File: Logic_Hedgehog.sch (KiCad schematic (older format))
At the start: 11 parts

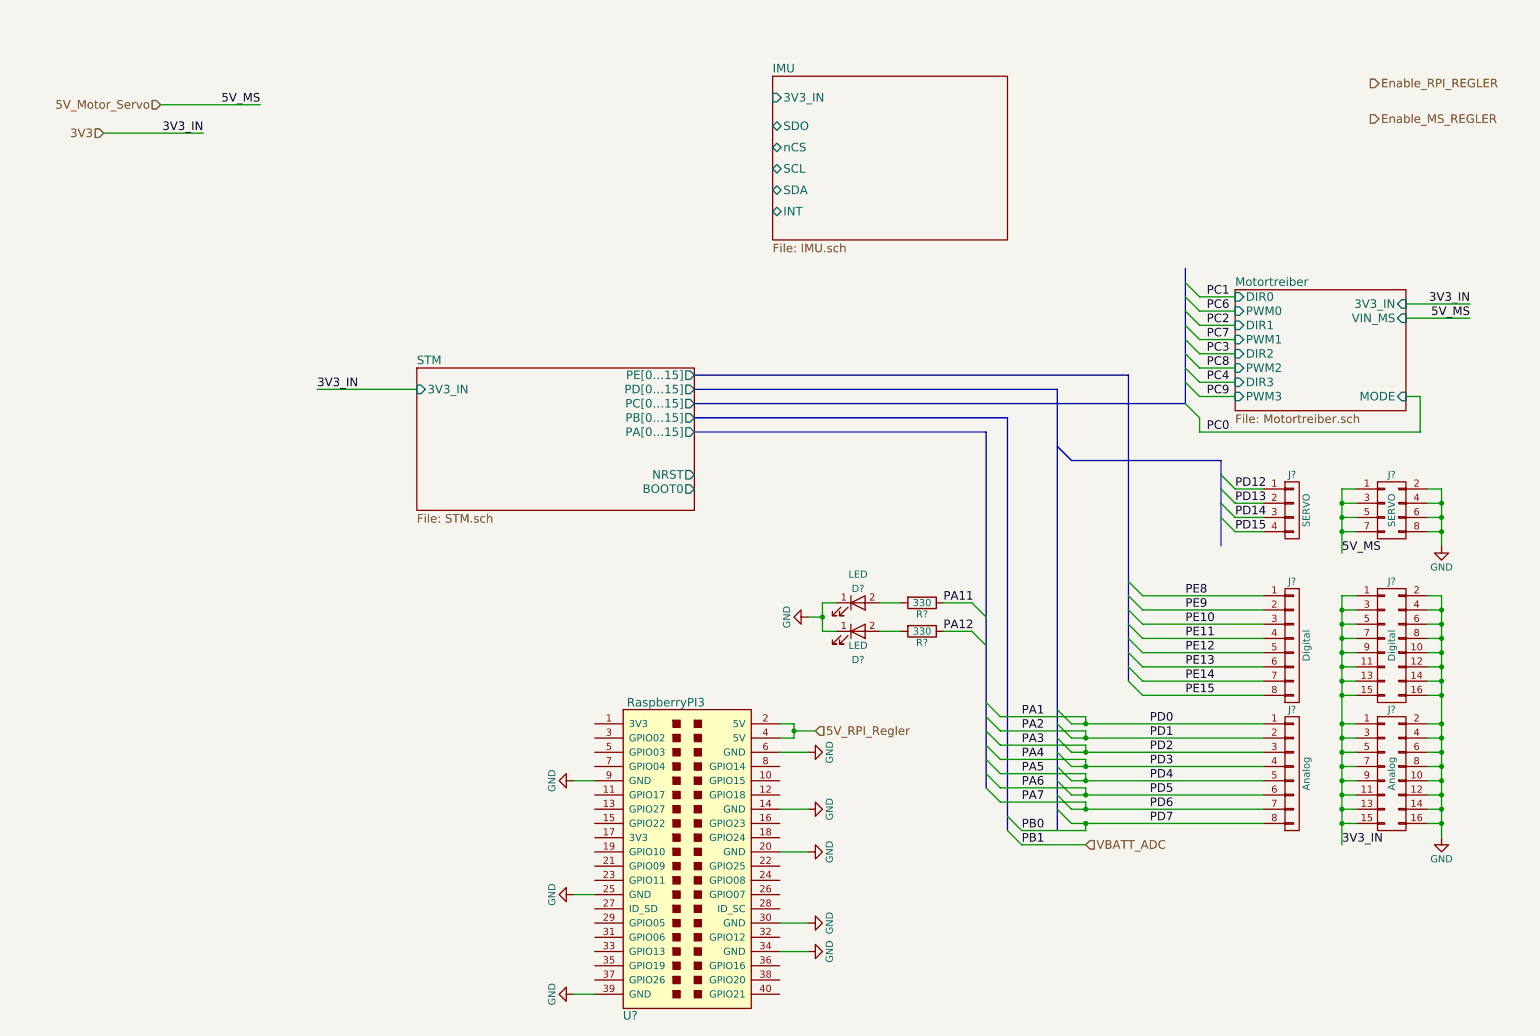
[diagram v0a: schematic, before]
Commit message: Added Piezo Buzzer in Libray Added Piezo Buzzer schematic Added Pinout for STM32 SWDIO / JTAG is missing
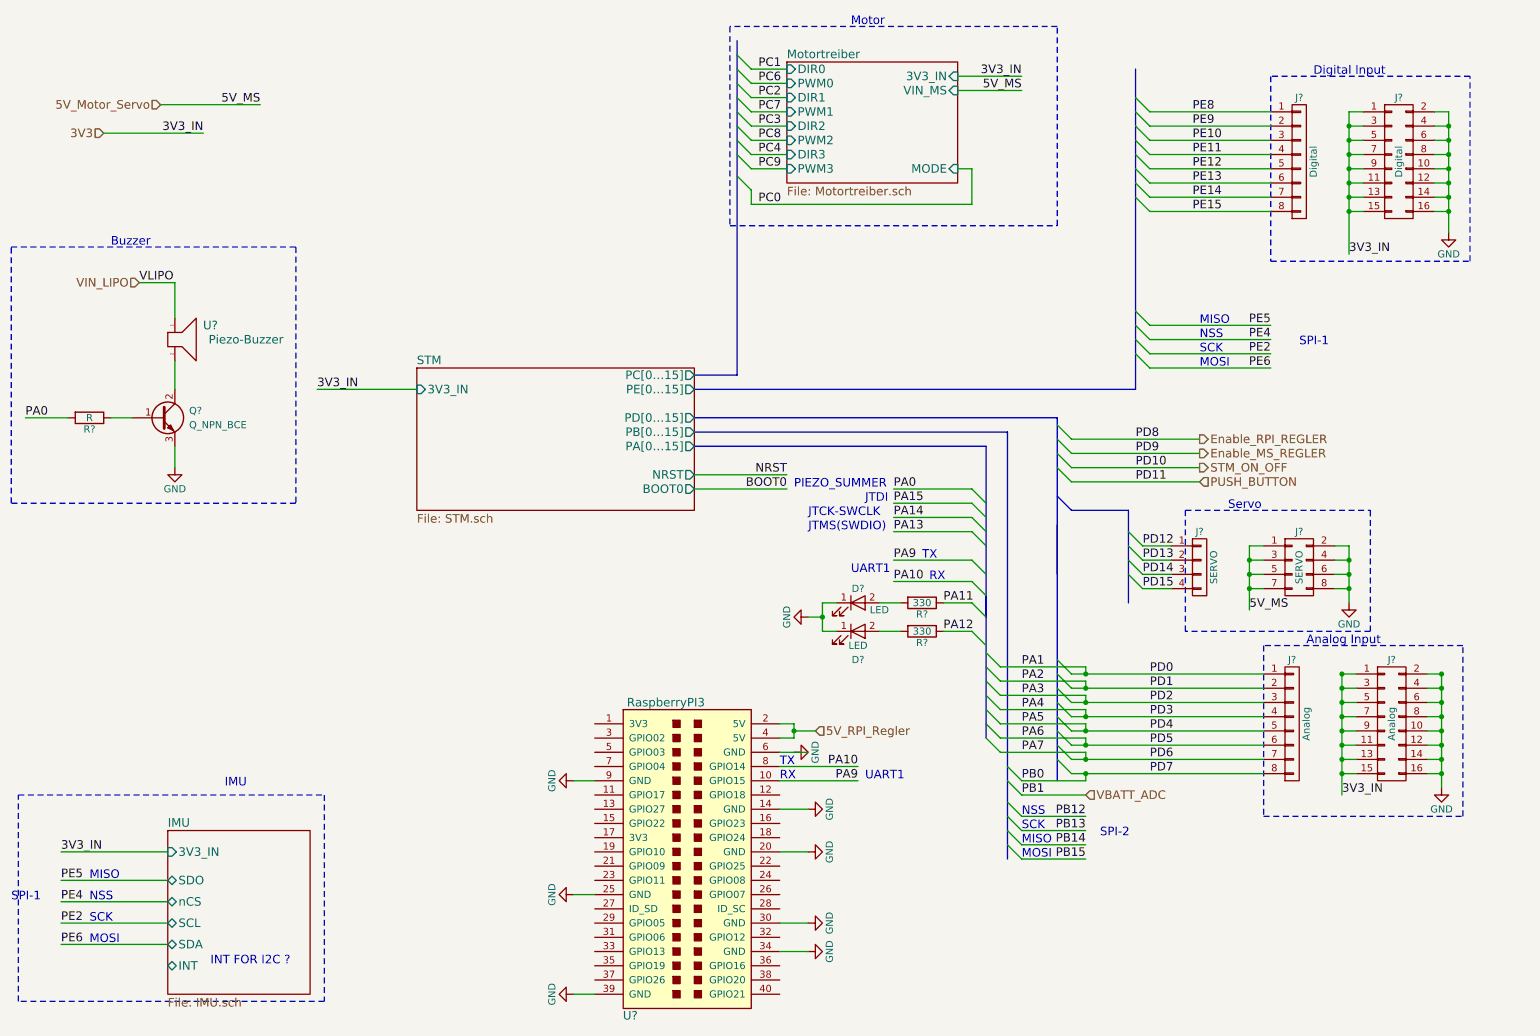
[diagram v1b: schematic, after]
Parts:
- added Q?: Q_NPN_BCE, symbol Q_NPN_BCE
- added R?: R, symbol R
- added U?: Piezo-Buzzer, symbol Piezo-Buzzer
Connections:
- net GND: now also Q?.3 (E); no longer U?.6 (GND)
- net PA9: now reaches U?.10 (GPIO15)
- net PA10: now reaches U?.8 (GPIO14)
- new net: Q?.2 (C), U?.2
- new net: Q?.1 (B), R?.1
- new net PA0: R?.2
- new net VIN_LIPO: U?.1
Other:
- note added: "Analog Input"
- note added: "Buzzer"
- note added: "Digital Input"
- note added: "IMU"
- note added: "INT FOR I2C ?"
- note added: "JTCK-SWCLK"
- note added: "JTDI"
- note added: "JTMS(SWDIO)"
- note added: "MISO"
- note added: "MOSI"
- note added: "Motor"
- note added: "NSS"
- note added: "PIEZO_SUMMER"
- note added: "RX"
- note added: "SCK"
- note added: "SPI-1"
- note added: "SPI-2"
- note added: "Servo"
- note added: "TX"
- note added: "UART1"
- moved on the sheet: J?

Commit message: cleanup
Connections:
- net VIN_LIPO is gone; now on net +3V3: U?.1
- net 3V3 renamed +3V3
- net 5V_Motor_Servo renamed +5V
- net 5V_RPI_Regler renamed 5V_RPi
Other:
- note added: "SPI1"
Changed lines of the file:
@@
 LIBS:valves
 LIBS:hedgehog_symbols
+LIBS:switches
 LIBS:Hedgehog-cache
-EELAYER 25 0
+EELAYER 26 0
 EELAYER END
 $Descr A4 11693 8268
@@
 $EndDescr
 Text HLabel 6350 5600 2    60   Input ~ 0
-5V_RPI_Regler
-Text HLabel 1750 1200 0    60   Input ~ 0
-5V_Motor_Servo
-Text HLabel 1350 1400 0    60   Input ~ 0
+5V_RPi
+Text HLabel 1700 1500 0    60   Input ~ 0
+5V_MS
+Text HLabel 1700 1775 0    60   Input ~ 0
 3V3
 Text HLabel 9050 3550 2    60   Output ~ 0
-Enable_RPI_REGLER
+EN_Reg_RPi
 Text HLabel 9050 3650 2    60   Output ~ 0
-Enable_MS_REGLER
+EN_Reg_MS
 $Sheet
 S 3550 3050 1950 1000
@@
 F12 "MODE" I R 7350 1650 60
 $EndSheet
-Text Label 2050 1400 2    60   ~ 0
-3V3_IN
-Text Label 2850 3200 0    60   ~ 0
-3V3_IN
-Text Label 7800 1000 2    60   ~ 0
-3V3_IN
-Text Label 2450 1200 2    60   ~ 0
-5V_MS
-Text Label 7800 1100 2    60   ~ 0
-5V_MS
 $Comp
 L RaspberryPI3 U?
@@
 	1    0    0    -1
 $EndComp
-Text Label 9400 4750 0    60   ~ 0
-5V_MS
 $Comp
 L GND #PWR?
@@
 	1    0    0    -1
 $EndComp
-Text Label 10050 6050 0    60   ~ 0
-3V3_IN
 Entry Wire Line
 	8600 1150 8700 1250
@@
 PB1
 Text HLabel 8250 6050 2    60   Input ~ 0
-VBATT_ADC
+POWER_IN_SENSE
 Entry Wire Line
 	5800 850  5900 950
@@
 $EndSheet
 Text HLabel 9050 3750 2    60   Output ~ 0
-STM_ON_OFF
+EN_PWR_IN
 Text HLabel 9050 3850 2    60   Input ~ 0
-PUSH_BUTTON
+PWR_BUTTON_STATE
 Text Notes 2100 7250 0    60   ~ 0
 INT FOR I2C ?
 Wire Wire Line
-	1350 1400 2050 1400
-Wire Wire Line
-	3550 3200 2850 3200
-Wire Wire Line
-	7350 1000 7800 1000
-Wire Wire Line
-	1750 1200 2450 1200
-Wire Wire Line
-	7350 1100 7800 1100
-Wire Wire Line
 	6100 5550 6200 5550
 Wire Wire Line
@@
 Wire Wire Line
 	9400 4600 9500 4600
-Wire Wire Line
-	9400 4300 9400 4750
 Wire Wire Line
 	9400 4300 9500 4300
@@
 Connection ~ 10050 5900
 Wire Wire Line
-	10100 1250 10100 2250
-Wire Wire Line
-	10050 5200 10050 6050
-Wire Wire Line
 	8700 1250 9550 1250
 Wire Wire Line
@@
 	1050 6800 1800 6800
 Wire Wire Line
-	1800 6450 1050 6450
-Wire Wire Line
 	1800 6650 1050 6650
 Wire Wire Line
@@
 Wire Wire Line
 	1800 7100 1050 7100
-Text Label 1050 6450 0    60   ~ 0
-3V3_IN
 Text Label 1050 6650 0    60   ~ 0
 PE5
@@
 	1    0    0    -1
 $EndComp
-Text Label 10100 2250 0    60   ~ 0
-3V3_IN
 Entry Wire Line
 	8050 3450 8150 3550
@@
 Text Notes 6600 4500 0    60   ~ 0
 UART1
-Text Notes 700  6800 0    60   ~ 0
-SPI-1
+Text Notes 775  6800 0    60   ~ 0
+SPI1
 Entry Wire Line
 	7700 6100 7800 6200
@@
 Wire Wire Line
 	1850 3600 1850 3750
-Wire Wire Line
-	1850 2700 1850 2450
 $Comp
 L R R?
@@
 Wire Wire Line
 	1100 3400 800  3400
-Wire Wire Line
-	1850 2450 1600 2450
-Text Label 1600 2450 0    60   ~ 0
-VLIPO
-Text HLabel 1600 2450 0    60   Input ~ 0
-VIN_LIPO
 Text Label 800  3400 0    60   ~ 0
 PA0
@@
 Wire Notes Line
 	700  2200 2700 2200
+$Comp
+L +3V3 #PWR?
+U 1 1 59094422
+P 1775 1725
+F 0 "#PWR?" H 1775 1575 50  0001 C CNN
+F 1 "+3V3" H 1775 1875 50  0000 C CNN
+F 2 "" H 1775 1725 50  0001 C CNN
+F 3 "" H 1775 1725 50  0001 C CNN
+	1    1775 1725
+	1    0    0    -1
+$EndComp
+Wire Wire Line
+	1775 1725 1775 1775
+Wire Wire Line
+	1775 1775 1700 1775
+$Comp
+L +3V3 #PWR?
+U 1 1 59094E31
+P 1850 2600
+F 0 "#PWR?" H 1850 2450 50  0001 C CNN
+F 1 "+3V3" H 1850 2750 50  0000 C CNN
+F 2 "" H 1850 2600 50  0001 C CNN
+F 3 "" H 1850 2600 50  0001 C CNN
+	1    1850 2600
+	1    0    0    -1
+$EndComp
+Wire Wire Line
+	1850 2600 1850 2700
+$Comp
+L +3V3 #PWR?
+U 1 1 590959B1
+P 3375 3125
+F 0 "#PWR?" H 3375 2975 50  0001 C CNN
+F 1 "+3V3" H 3375 3275 50  0000 C CNN
+F 2 "" H 3375 3125 50  0001 C CNN
+F 3 "" H 3375 3125 50  0001 C CNN
+	1    3375 3125
+	1    0    0    -1
+$EndComp
+Wire Wire Line
+	3375 3125 3375 3200
+Wire Wire Line
+	3375 3200 3550 3200
+$Comp
+L +3V3 #PWR?
+U 1 1 59095ED7
+P 1575 6375
+F 0 "#PWR?" H 1575 6225 50  0001 C CNN
+F 1 "+3V3" H 1575 6525 50  0000 C CNN
+F 2 "" H 1575 6375 50  0001 C CNN
+F 3 "" H 1575 6375 50  0001 C CNN
+	1    1575 6375
+	1    0    0    -1
+$EndComp
+Wire Wire Line
+	1575 6375 1575 6450
+Wire Wire Line
+	1575 6450 1800 6450
+$Comp
+L +3V3 #PWR?
+U 1 1 59096BAF
+P 10050 5150
+F 0 "#PWR?" H 10050 5000 50  0001 C CNN
+F 1 "+3V3" H 10175 5250 50  0000 C CNN
+F 2 "" H 10050 5150 50  0001 C CNN
+F 3 "" H 10050 5150 50  0001 C CNN
+	1    10050 5150
+	1    0    0    -1
+$EndComp
+Wire Wire Line
+	10050 5150 10050 5900
+$Comp
+L +3V3 #PWR?
+U 1 1 5909B6DB
+P 10100 1200
+F 0 "#PWR?" H 10100 1050 50  0001 C CNN
+F 1 "+3V3" H 10100 1350 50  0000 C CNN
+F 2 "" H 10100 1200 50  0001 C CNN
+F 3 "" H 10100 1200 50  0001 C CNN
+	1    10100 1200
+	1    0    0    -1
+$EndComp
+Connection ~ 10100 1250
+Wire Wire Line
+	10100 1200 10100 1950
+$Comp
+L +3V3 #PWR?
+U 1 1 5909E6BA
+P 7450 925
+F 0 "#PWR?" H 7450 775 50  0001 C CNN
+F 1 "+3V3" H 7450 1075 50  0000 C CNN
+F 2 "" H 7450 925 50  0001 C CNN
+F 3 "" H 7450 925 50  0001 C CNN
+	1    7450 925
+	1    0    0    -1
+$EndComp
+Wire Wire Line
+	7450 925  7450 1000
+Wire Wire Line
+	7450 1000 7350 1000
+$Comp
+L +5V #PWR?
+U 1 1 590A3BB0
+P 1775 1450
+F 0 "#PWR?" H 1775 1300 50  0001 C CNN
+F 1 "+5V" H 1775 1600 50  0000 C CNN
+F 2 "" H 1775 1450 50  0001 C CNN
+F 3 "" H 1775 1450 50  0001 C CNN
+	1    1775 1450
+	1    0    0    -1
+$EndComp
+Wire Wire Line
+	1700 1500 1775 1500
+Wire Wire Line
+	1775 1500 1775 1450
+$Comp
+L +5V #PWR?
+U 1 1 590A40B0
+P 7650 925
+F 0 "#PWR?" H 7650 775 50  0001 C CNN
+F 1 "+5V" H 7650 1075 50  0000 C CNN
+F 2 "" H 7650 925 50  0001 C CNN
+F 3 "" H 7650 925 50  0001 C CNN
+	1    7650 925
+	1    0    0    -1
+$EndComp
+Wire Wire Line
+	7650 925  7650 1100
+Wire Wire Line
+	7650 1100 7350 1100
+$Comp
+L +5V #PWR?
+U 1 1 590A66E3
+P 9400 4250
+F 0 "#PWR?" H 9400 4100 50  0001 C CNN
+F 1 "+5V" H 9400 4400 50  0000 C CNN
+F 2 "" H 9400 4250 50  0001 C CNN
+F 3 "" H 9400 4250 50  0001 C CNN
+	1    9400 4250
+	1    0    0    -1
+$EndComp
+Wire Wire Line
+	9400 4250 9400 4600
+Connection ~ 9400 4300
 $EndSCHEMATC

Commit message: more cleanup
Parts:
- removed Q?: Q_NPN_BCE, symbol Q_NPN_BCE
- removed R?: R, symbol R
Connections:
- net +3V3: no longer U?.1
- net PA0: now also U?.1
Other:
- note added: "Piezo-Buzzer"
- note added: "Problem: 2 net names"
- note added: "SPI2"
- note added: "TODO: Timer1"
- note removed: "PIEZO_SUMMER"
- note removed: "SPI-1"
- note removed: "SPI-2"
- moved on the sheet: U?
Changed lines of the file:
@@
 S 6150 900  1200 850
 U 58F5B6C4
-F0 "Motortreiber" 60
-F1 "Motortreiber.sch" 60
+F0 "Motor_Drivers" 60
+F1 "Motor_Drivers.sch" 60
 F2 "3V3_IN" I R 7350 1000 60
 F3 "VIN_MS" I R 7350 1100 60
-F4 "DIR0" I L 6150 950 60
-F5 "DIR1" I L 6150 1150 60
-F6 "DIR2" I L 6150 1350 60
-F7 "DIR3" I L 6150 1550 60
-F8 "PWM0" I L 6150 1050 60
-F9 "PWM1" I L 6150 1250 60
-F10 "PWM2" I L 6150 1450 60
-F11 "PWM3" I L 6150 1650 60
-F12 "MODE" I R 7350 1650 60
+F4 "M0_1" I L 6150 950 60
+F5 "M1_1" I L 6150 1150 60
+F6 "M2_1" I L 6150 1350 60
+F7 "M3_1" I L 6150 1550 60
+F8 "M0_2" I L 6150 1050 60
+F9 "M1_2" I L 6150 1250 60
+F10 "M2_2" I L 6150 1450 60
+F11 "M3_2" I L 6150 1650 60
+F12 "MODE01" I R 7350 1650 60
+F13 "MODE23" I R 7350 1550 60
 $EndSheet
 $Comp
@@
 Entry Wire Line
 	5800 1550 5900 1650
-Entry Wire Line
-	5800 1700 5900 1800
 Text Label 5950 1900 0    60   ~ 0
 PC0
@@
 	5900 1650 6150 1650
 Wire Wire Line
-	5900 1800 5900 1900
-Wire Wire Line
 	5900 1900 7450 1900
 Wire Wire Line
@@
 Text Label 8250 6500 2    60   ~ 0
 PB15
-Text Notes 8350 6350 0    60   ~ 0
-SPI-2
+Text Notes 8300 6350 0    60   ~ 0
+SPI2
 Text Notes 7100 4400 0    60   ~ 0
 TX
@@
 Text Notes 9050 3050 0    60   ~ 0
 MOSI
-Text Notes 9750 2900 0    60   ~ 0
-SPI-1
+Text Notes 9600 2900 0    60   ~ 0
+SPI1
 Wire Wire Line
 	5500 3900 6150 3900
@@
 Text Label 6900 3900 0    60   ~ 0
 PA0
-Text Notes 6200 3900 0    60   ~ 0
-PIEZO_SUMMER
+Text Notes 6275 3900 0    60   ~ 0
+Piezo-Buzzer
 $Comp
 L Piezo-Buzzer U?
 U 1 1 58FC2F9F
-P 1900 2850
-F 0 "U?" H 2100 2950 60  0000 C CNN
-F 1 "Piezo-Buzzer" H 2350 2850 60  0000 C CNN
-F 2 "" H 1900 2850 60  0001 C CNN
-F 3 "" H 1900 2850 60  0001 C CNN
-	1    1900 2850
-	1    0    0    -1
-$EndComp
-$Comp
-L Q_NPN_BCE Q?
-U 1 1 58FC3920
-P 1750 3400
-F 0 "Q?" H 1950 3450 50  0000 L CNN
-F 1 "Q_NPN_BCE" H 1950 3350 50  0000 L CNN
-F 2 "" H 1950 3500 50  0001 C CNN
-F 3 "" H 1750 3400 50  0001 C CNN
-	1    1750 3400
-	1    0    0    -1
-$EndComp
-Wire Wire Line
-	1850 3000 1850 3200
-Wire Wire Line
-	1550 3400 1400 3400
-$Comp
-L GND #PWR?
-U 1 1 58FC43D7
-P 1850 3750
-F 0 "#PWR?" H 1850 3500 50  0001 C CNN
-F 1 "GND" H 1850 3600 50  0000 C CNN
-F 2 "" H 1850 3750 50  0001 C CNN
-F 3 "" H 1850 3750 50  0001 C CNN
-	1    1850 3750
-	1    0    0    -1
-$EndComp
-Wire Wire Line
-	1850 3600 1850 3750
-$Comp
-L R R?
-U 1 1 58FC530A
-P 1250 3400
-F 0 "R?" V 1330 3400 50  0000 C CNN
-F 1 "R" V 1250 3400 50  0000 C CNN
-F 2 "" V 1180 3400 50  0001 C CNN
-F 3 "" H 1250 3400 50  0001 C CNN
-	1    1250 3400
-	0    1    1    0
-$EndComp
-Wire Wire Line
-	1100 3400 800  3400
-Text Label 800  3400 0    60   ~ 0
+P 1750 3075
+F 0 "U?" H 1950 3175 60  0000 C CNN
+F 1 "Piezo-Buzzer" H 2200 3075 60  0000 C CNN
+F 2 "" H 1750 3075 60  0001 C CNN
+F 3 "" H 1750 3075 60  0001 C CNN
+	1    1750 3075
+	1    0    0    -1
+$EndComp
+Text Label 1400 2850 0    60   ~ 0
 PA0
 Text Notes 9850 1000 0    60   ~ 0
@@
 $Comp
 L +3V3 #PWR?
-U 1 1 59094E31
-P 1850 2600
-F 0 "#PWR?" H 1850 2450 50  0001 C CNN
-F 1 "+3V3" H 1850 2750 50  0000 C CNN
-F 2 "" H 1850 2600 50  0001 C CNN
-F 3 "" H 1850 2600 50  0001 C CNN
-	1    1850 2600
-	1    0    0    -1
-$EndComp
-Wire Wire Line
-	1850 2600 1850 2700
-$Comp
-L +3V3 #PWR?
 U 1 1 590959B1
 P 3375 3125
@@
 	9400 4250 9400 4600
 Connection ~ 9400 4300
+Wire Wire Line
+	1700 2925 1700 2850
+Wire Wire Line
+	1700 2850 1400 2850
+Wire Wire Line
+	1700 3225 1700 3300
+Wire Wire Line
+	1700 3300 1400 3300
+Text Notes 7850 5000 0    60   ~ 0
+Problem: 2 net names
+Text Notes 1300 3525 0    60   ~ 0
+TODO: Timer1
+Entry Wire Line
+	5800 1900 5900 2000
+Wire Wire Line
+	5900 2000 7550 2000
+Wire Wire Line
+	7550 2000 7550 1550
+Wire Wire Line
+	7550 1550 7350 1550
+Text Label 5950 2000 0    60   ~ 0
+PC5
+Entry Wire Line
+	5800 1800 5900 1900
 $EndSCHEMATC

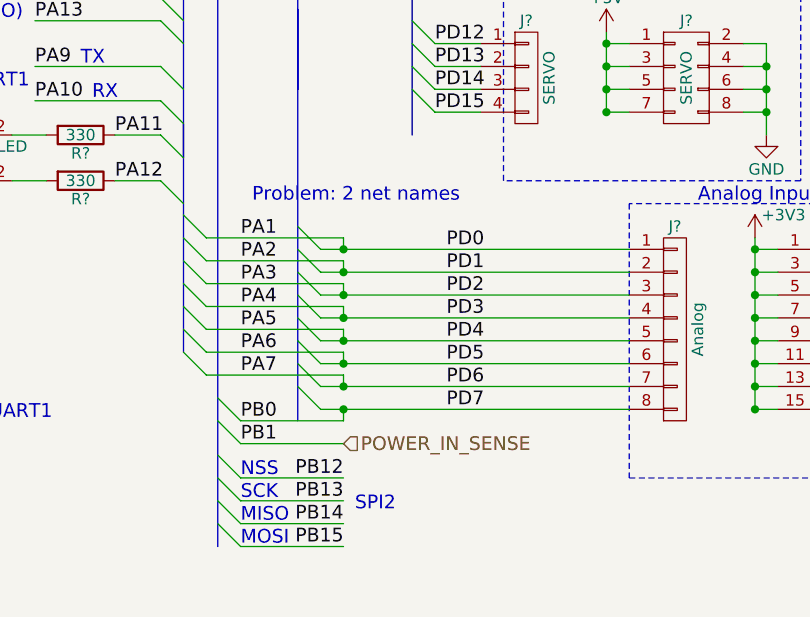
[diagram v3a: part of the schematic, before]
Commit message: added mosfet footprint some more cleanup
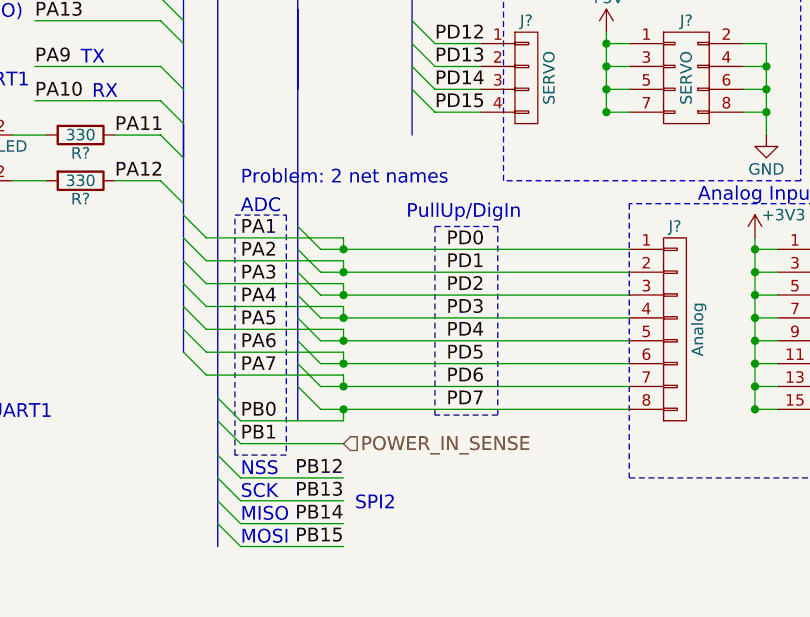
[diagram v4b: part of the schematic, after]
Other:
- note added: "ADC"
- note added: "PullUp/DigIn"

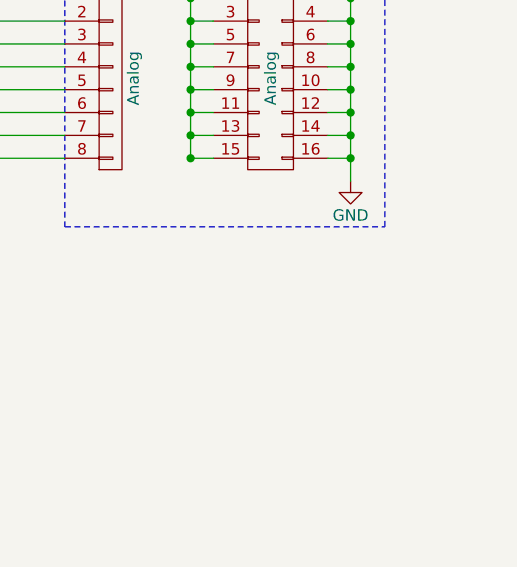
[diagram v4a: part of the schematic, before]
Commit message: added RPi Regulator added ref.des.-prefixes to all schematic sheets
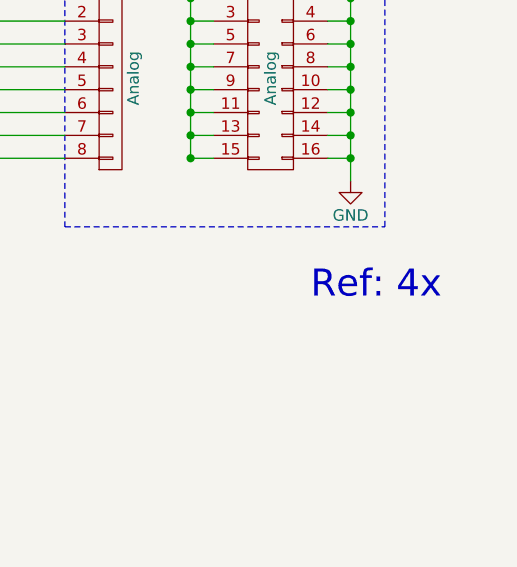
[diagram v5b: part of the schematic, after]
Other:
- note added: "Ref: 4x"
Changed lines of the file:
@@
 Text Notes 7800 5050 0    60   ~ 0
 ADC
+Text Notes 10575 6525 0    118  ~ 0
+Ref: 4x
 $EndSCHEMATC
